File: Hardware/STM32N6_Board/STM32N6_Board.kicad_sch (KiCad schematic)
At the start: 0 parts

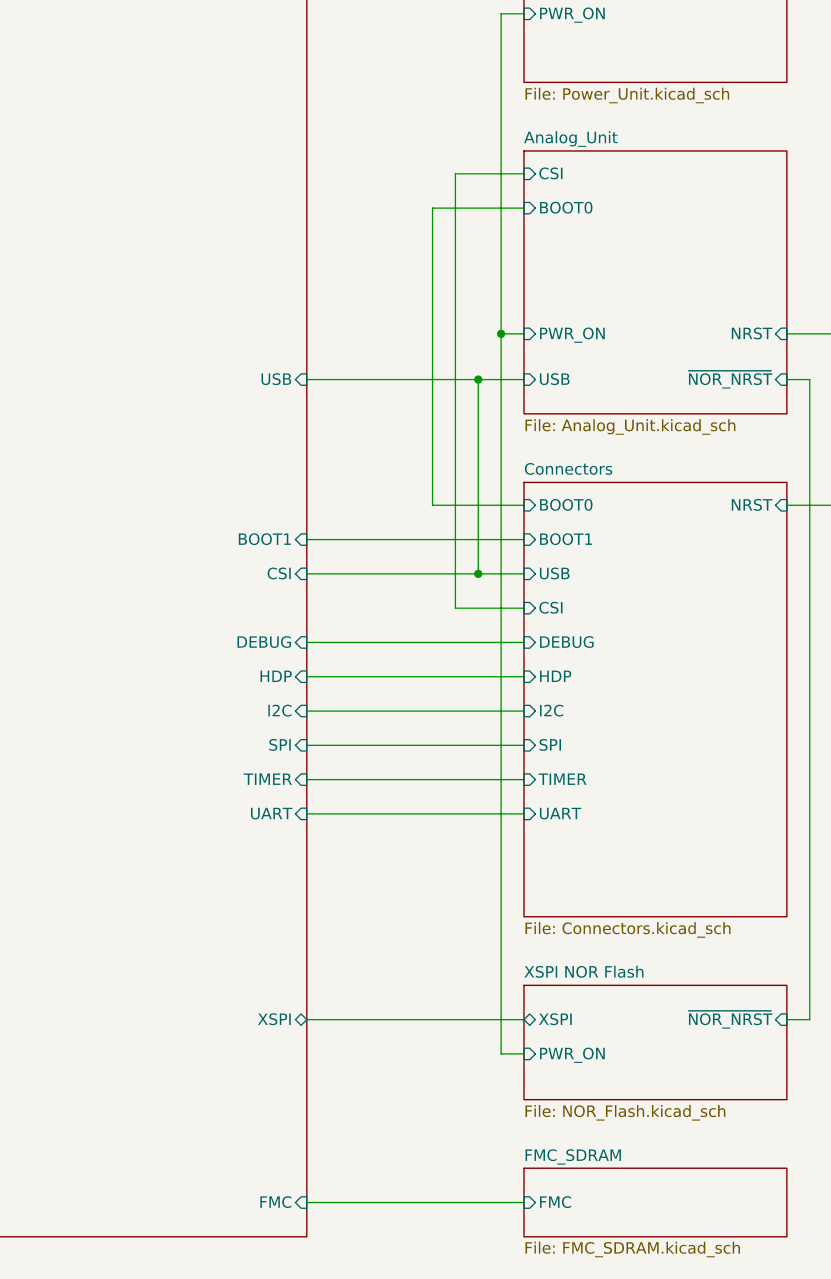
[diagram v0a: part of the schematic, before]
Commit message: Made fixes to remove ERC errors
- 1 remaining error, but > 100 warnings D:
- The remaining error is a bug within KiCAD I believe
- Next is footprint assignment
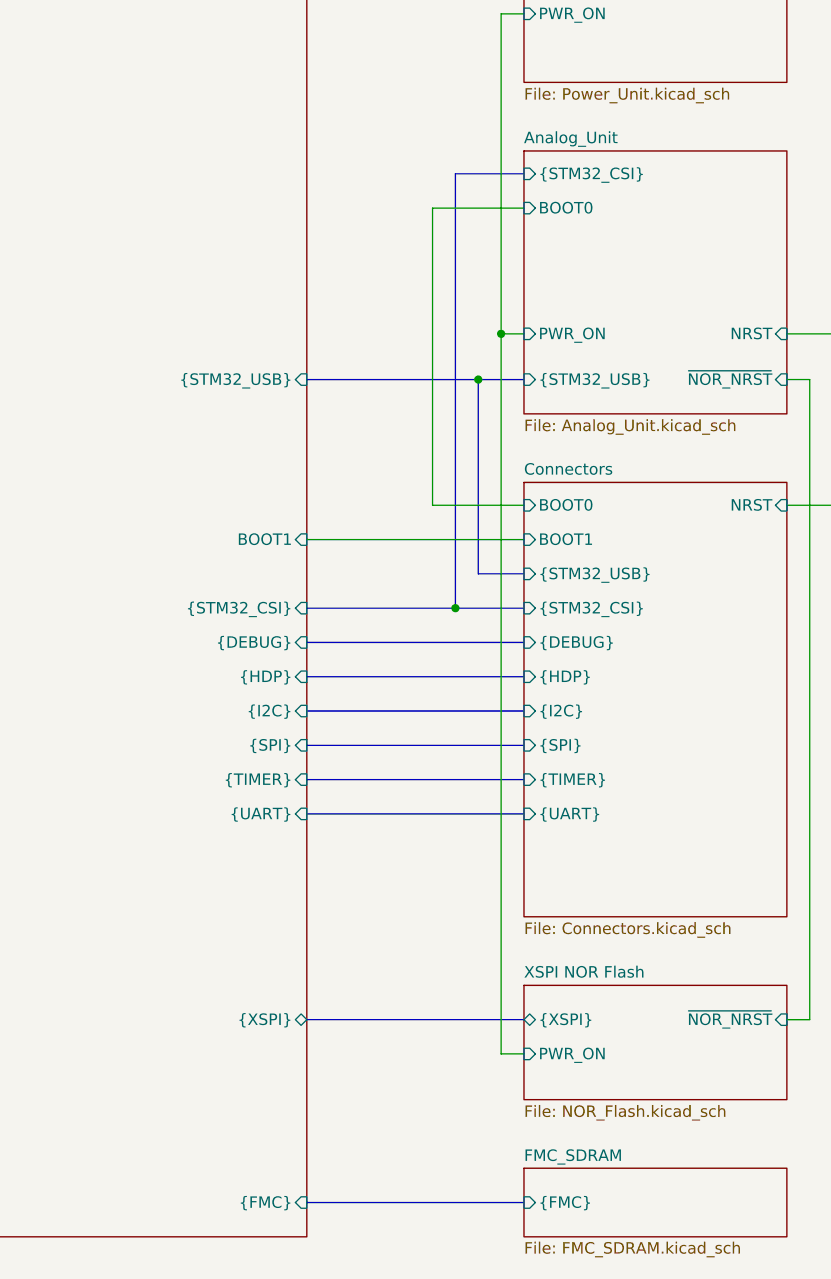
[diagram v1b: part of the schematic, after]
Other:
- sheet Analog_Unit ports: added {STM32_CSI}, {STM32_USB}; removed CSI, USB
- sheet Connectors ports: added {DEBUG}, {HDP}, {I2C}, {SPI}, {STM32_CSI}, {STM32_USB}, {TIMER}, {UART}; removed CSI, DEBUG, HDP, I2C, SPI, TIMER, UART, USB
- sheet FMC_SDRAM ports: added {FMC}; removed FMC
- sheet GPIO ports: added {DEBUG}, {FMC}, {HDP}, {I2C}, {SPI}, {STM32_CSI}, {STM32_USB}, {TIMER}, {UART}, {XSPI}; removed CSI, DEBUG, FMC, HDP, I2C, SPI, TIMER, UART, USB, XSPI
- sheet XSPI NOR Flash ports: added {XSPI}; removed XSPI

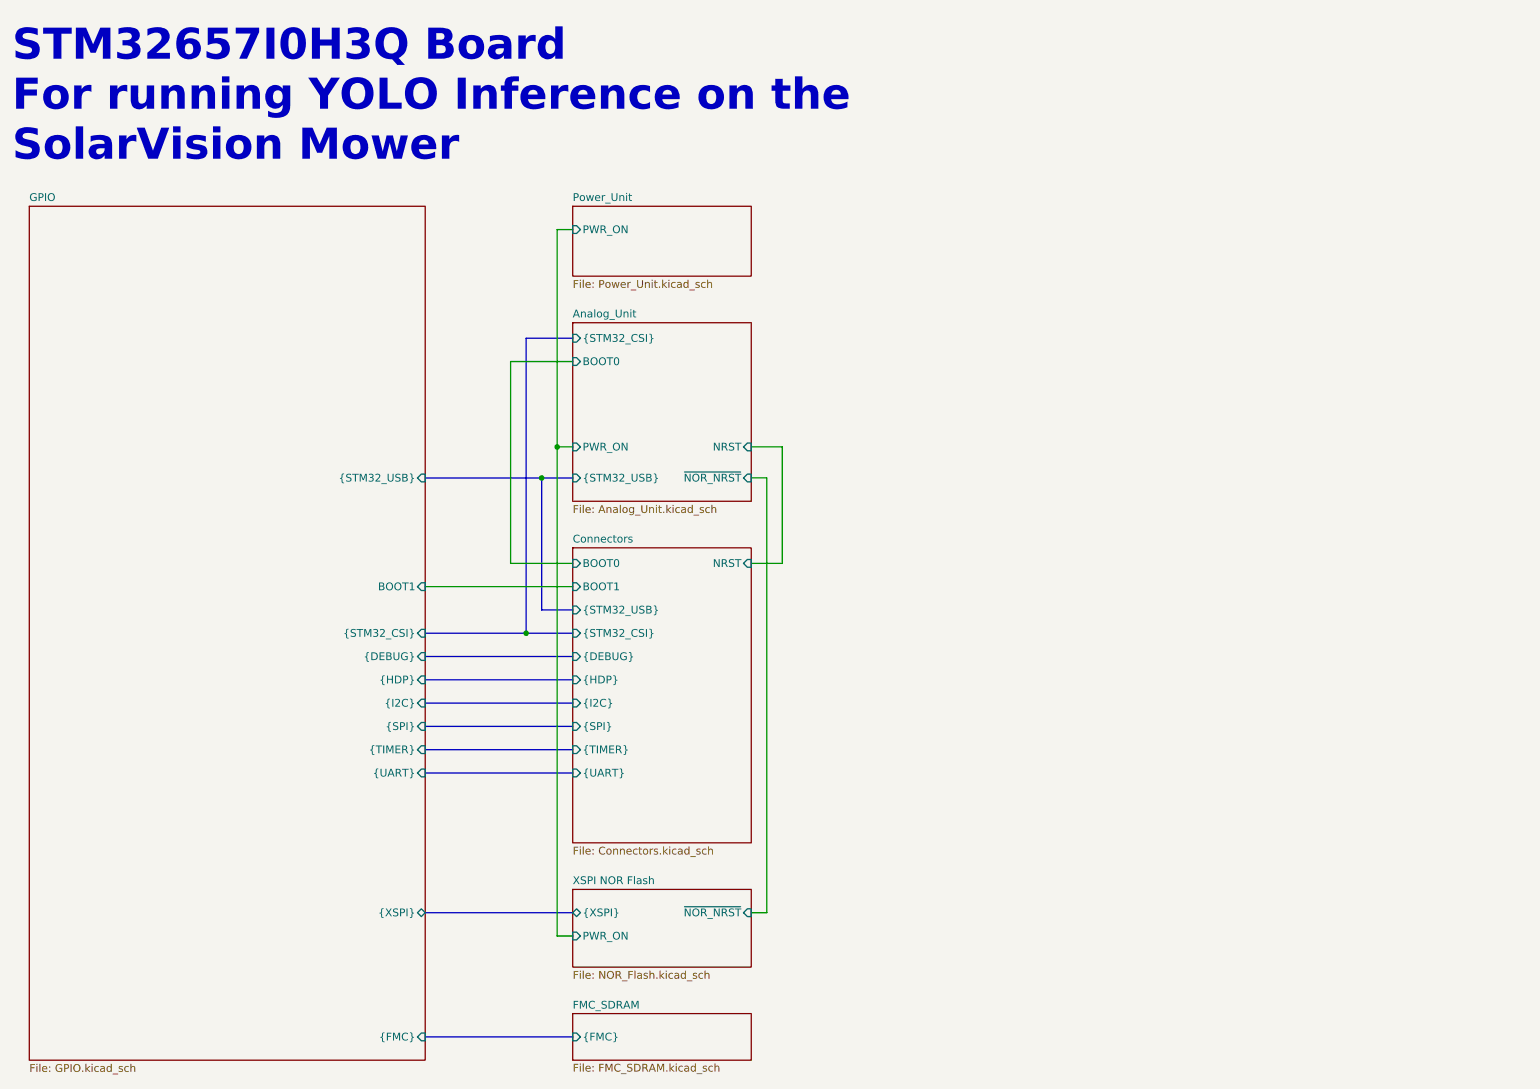
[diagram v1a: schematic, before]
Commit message: Completed a lot of the layout of the STM Board
- Major layout complete, but all the wiring still left. 488 open nets!
- The STM32's BGA fanout is complete, now comes laying out traces
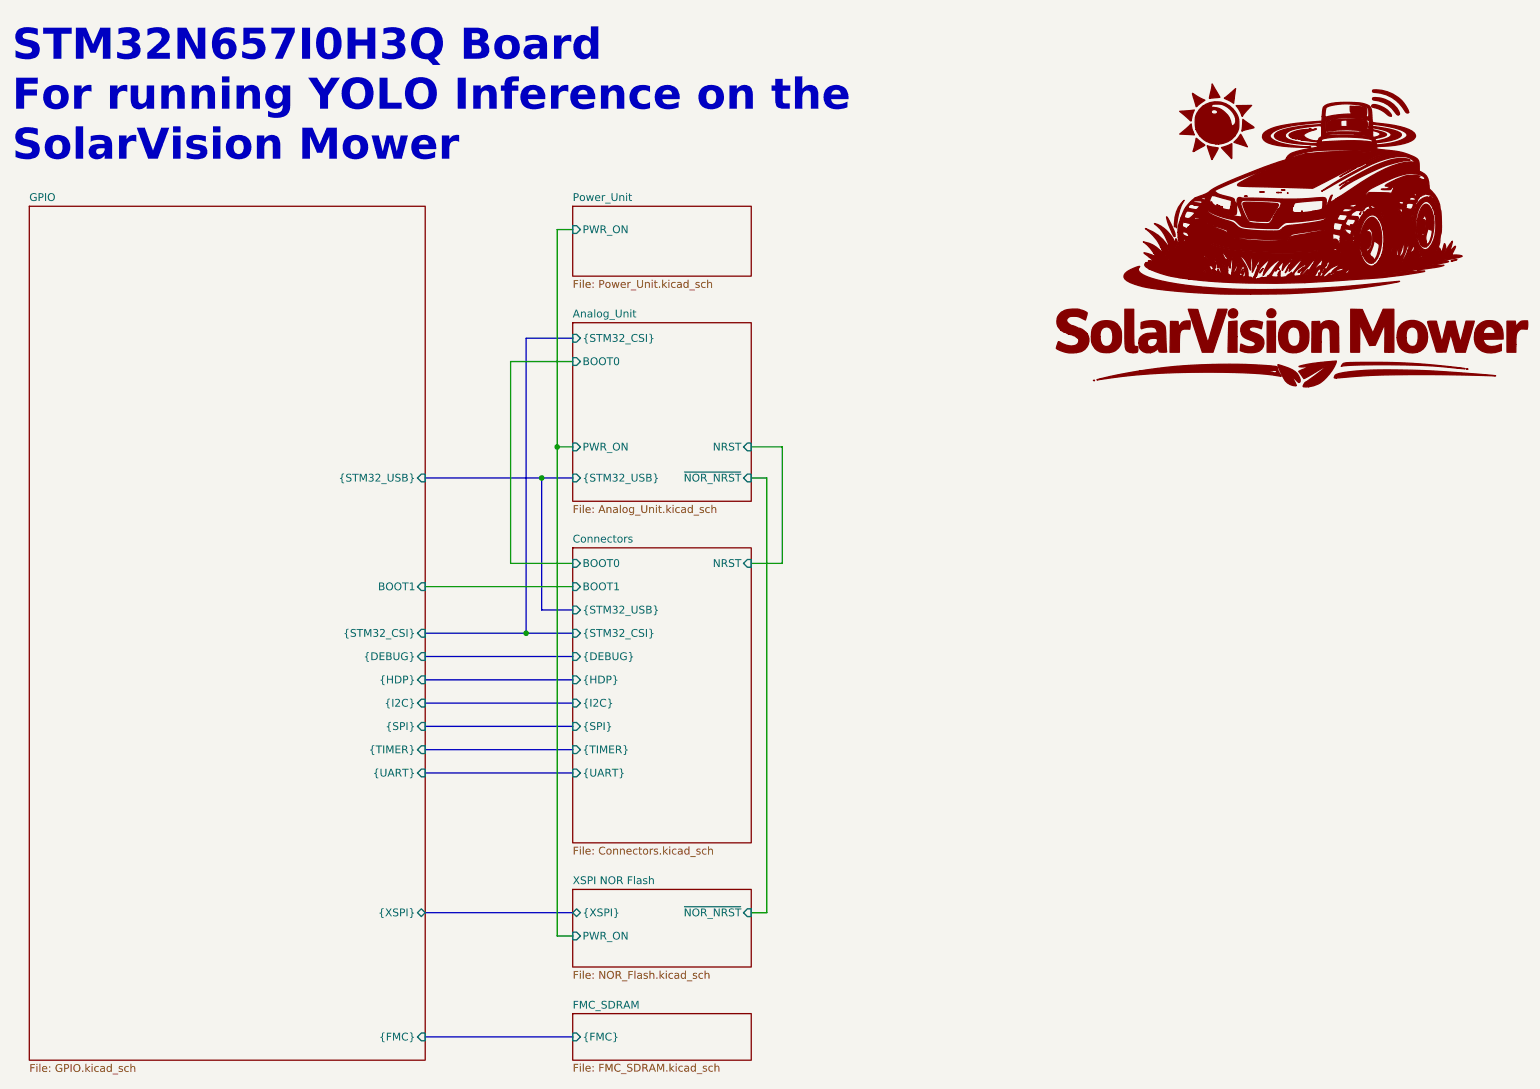
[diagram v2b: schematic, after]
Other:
- note added: "STM32N657I0H3Q Board For running YOLO Inference on the SolarVision Mower"
- note removed: "STM32657I0H3Q Board For running YOLO Inference on the SolarVision Mower"
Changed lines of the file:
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@@
 		(comment 1 "https://github.com/SolarVisionMower/SolarVision")
 	)
-	(text "STM32657I0H3Q Board\nFor running YOLO Inference on the\nSolarVision Mower"
+	(text "STM32N657I0H3Q Board\nFor running YOLO Inference on the\nSolarVision Mower"
 		(exclude_from_sim no)
 		(at 18.796 19.05 0)
@@
 		)
 	)
+	(symbol
+		(lib_id "Logo:LOGO")
+		(at 228.6 53.34 0)
+		(unit 1)
+		(exclude_from_sim no)
+		(in_bom yes)
+		(on_board yes)
+		(dnp no)
+		(fields_autoplaced yes)
+		(property "Reference" "#G1"
+			(at 228.6 27.2203 0)
+			(effects
+				(font
+					(size 1.27 1.27)
+				)
+				(hide yes)
+			)
+		)
+		(property "Value" "LOGO"
+			(at 228.6 79.4597 0)
+			(effects
+				(font
+					(size 1.27 1.27)
+				)
+				(hide yes)
+			)
+		)
+		(property "Footprint" ""
+			(at 228.6 53.34 0)
+			(effects
+				(font
+					(size 1.27 1.27)
+				)
+				(hide yes)
+			)
+		)
+		(property "Datasheet" ""
+			(at 228.6 53.34 0)
+			(effects
+				(font
+					(size 1.27 1.27)
+				)
+				(hide yes)
+			)
+		)
+		(property "Description" ""
+			(at 228.6 53.34 0)
+			(effects
+				(font
+					(size 1.27 1.27)
+				)
+				(hide yes)
+			)
+		)
+		(instances
+			(project ""
+				(path "/4869b3db-9bd3-4900-9c3c-205f01100fa6"
+					(reference "#G1")
+					(unit 1)
+				)
+			)
+		)
+	)
